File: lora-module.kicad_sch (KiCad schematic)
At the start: 12 parts, among them J101 Conn_Coaxial, J102 Conn_ARM_SWD_TagConnect_TC203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, J103 Conn_01x07_Socket, J104 Conn_01x07_Socket, J105 Conn_01x07_Socket, Q101 PMN48XP

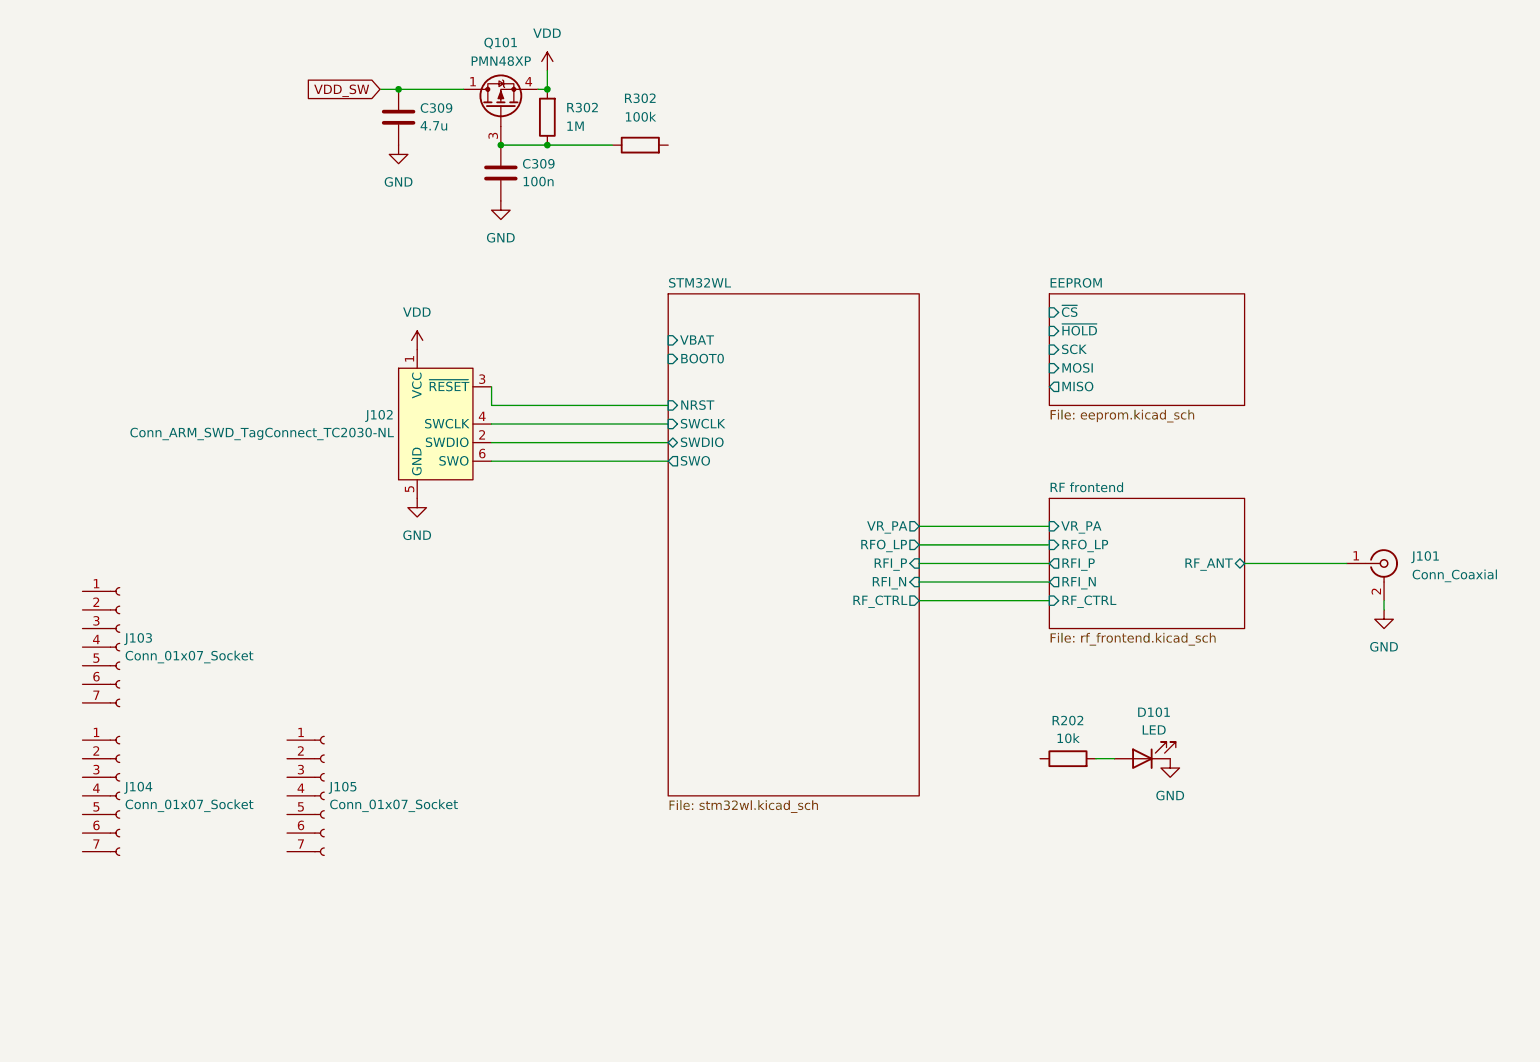
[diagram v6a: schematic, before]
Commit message: created a footprint for the edge connectors
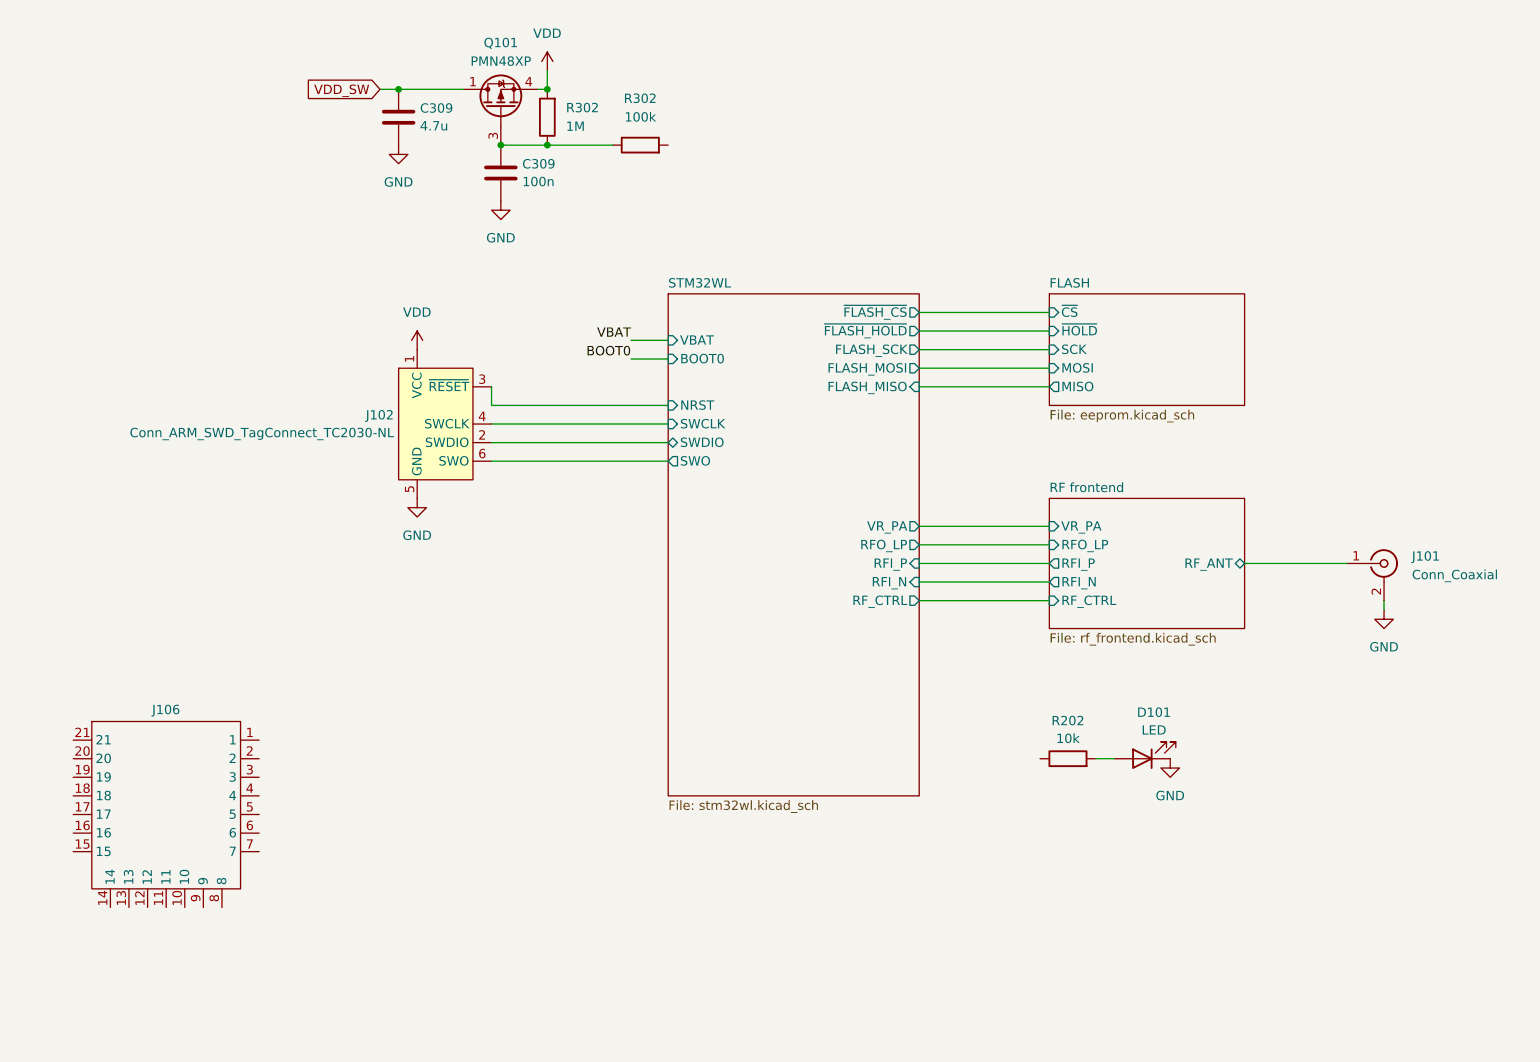
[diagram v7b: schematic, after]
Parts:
- removed J103, J104, J105: Conn_01x07_Socket, Connector_PinSocket_2.54mm:PinSocket_1x07_P2.54mm_Vertical, symbol Connector:Conn_01x07_Socket
- added J106: ~, lora-module:module-connectors, symbol lora-module:module-connectors
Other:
- sheet EEPROM renamed FLASH
- sheet STM32WL ports: added FLASH_MISO, FLASH_MOSI, FLASH_SCK, ~{FLASH_CS}, ~{FLASH_HOLD}; removed none

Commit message: mostly finishing, all IOs connected, drc clean
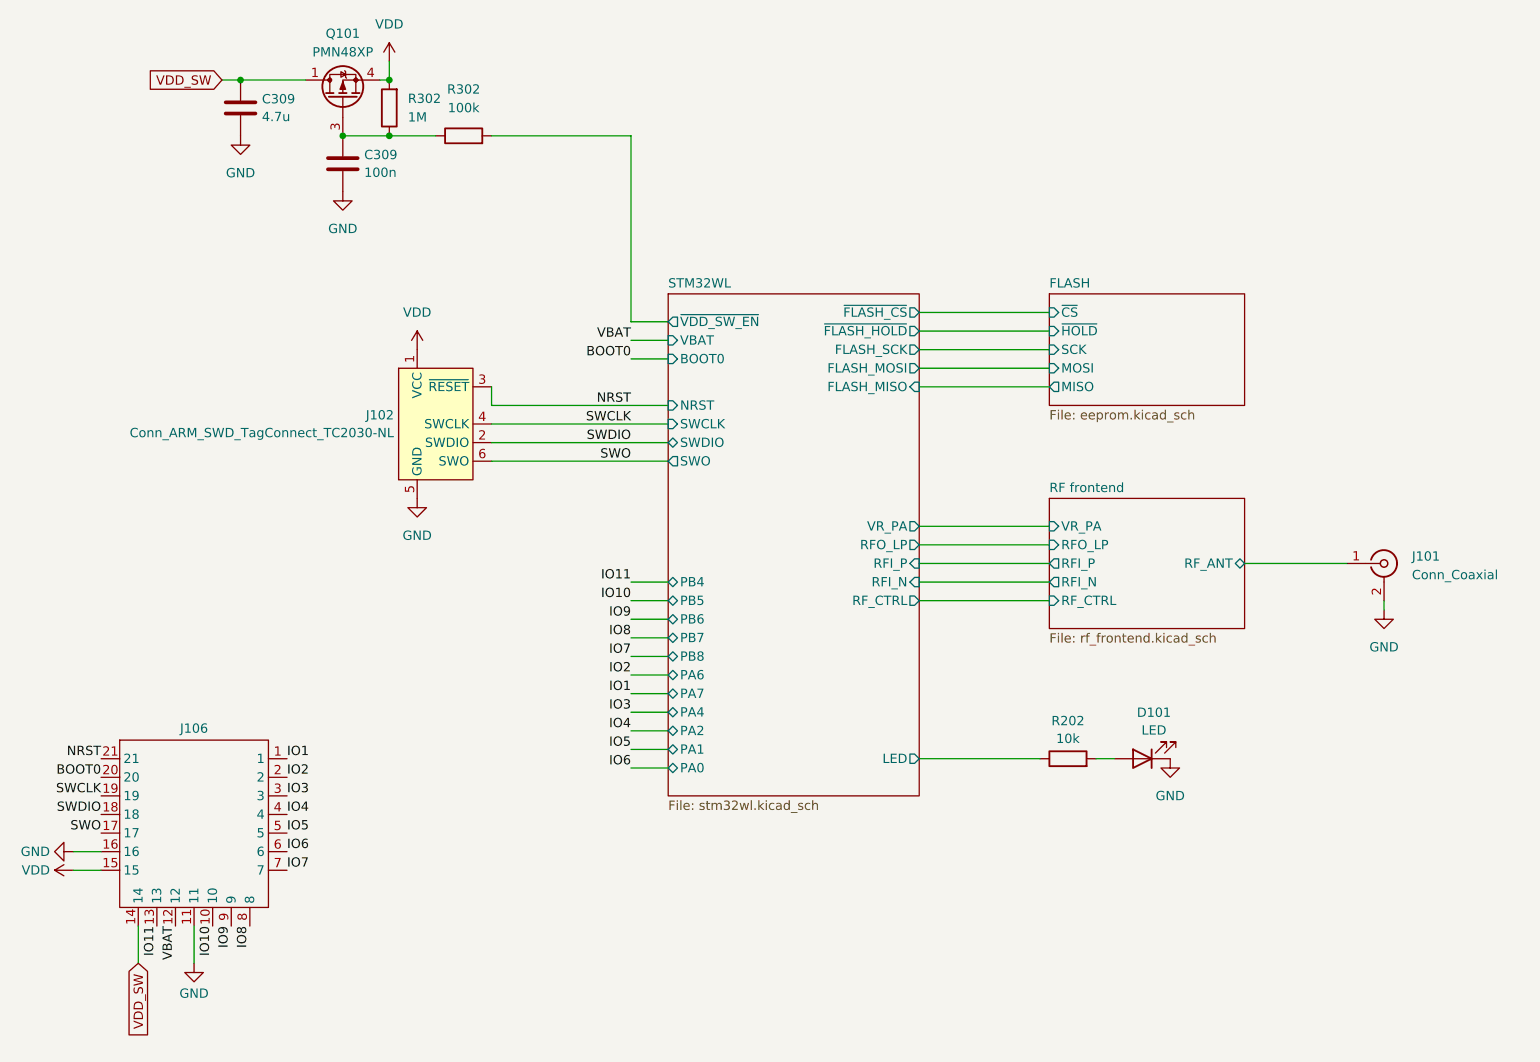
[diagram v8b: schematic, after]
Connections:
- net STM32WL/NRST is gone; now on net NRST: J102.3 (~{RESET})
- net STM32WL/SWCLK is gone; now on net SWCLK: J102.4 (SWCLK)
- net STM32WL/SWDIO is gone; now on net SWDIO: J102.2 (SWDIO)
- net STM32WL/SWO is gone; now on net SWO: J102.6 (SWO)
- net BOOT0: now also J106.20
- net GND: now also J106.11, J106.16
- net VBAT: now also J106.12
- net VDD: now also J106.15
- net VDD_SW: now also J106.14
- net IO1: now reaches J106.1
- net IO10: now reaches J106.10
- net IO11: now reaches J106.13
- net SWO: now reaches J106.17
- net SWDIO: now reaches J106.18
- net SWCLK: now reaches J106.19
- net IO2: now reaches J106.2
- net NRST: now reaches J106.21
- net IO3: now reaches J106.3
- net IO4: now reaches J106.4
- net IO5: now reaches J106.5
- net IO6: now reaches J106.6
- net IO7: now reaches J106.7
- net IO8: now reaches J106.8
- net IO9: now reaches J106.9
- net STM32WL/~{VDD_SW_EN}: now reaches R302.2
- net STM32WL/LED: now reaches R202.1
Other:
- sheet STM32WL ports: added LED, PA0, PA1, PA2, PA4, PA6, PA7, PB4, PB5, PB6, PB7, PB8, ~{VDD_SW_EN}; removed none
- moved on the sheet: C309, J106, Q101, R302
